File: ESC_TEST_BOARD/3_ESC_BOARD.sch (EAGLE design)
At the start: 63 parts, among them J3 AVR_SPI_PROG_3X2NS, U2 ATMEGA328P_TQFP

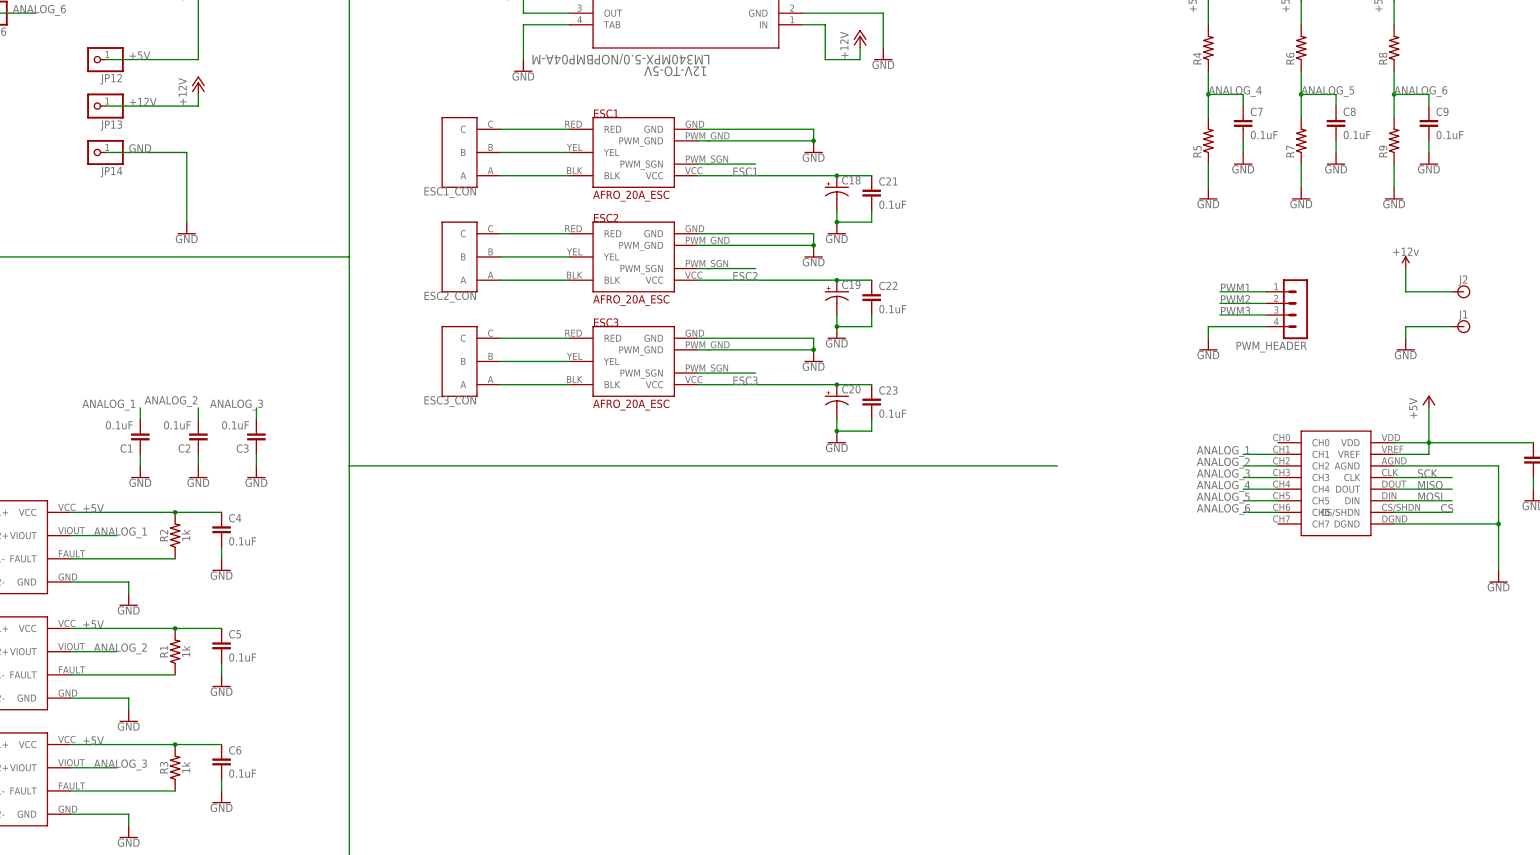
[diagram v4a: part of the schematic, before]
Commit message: Finished routing of Jacobs section
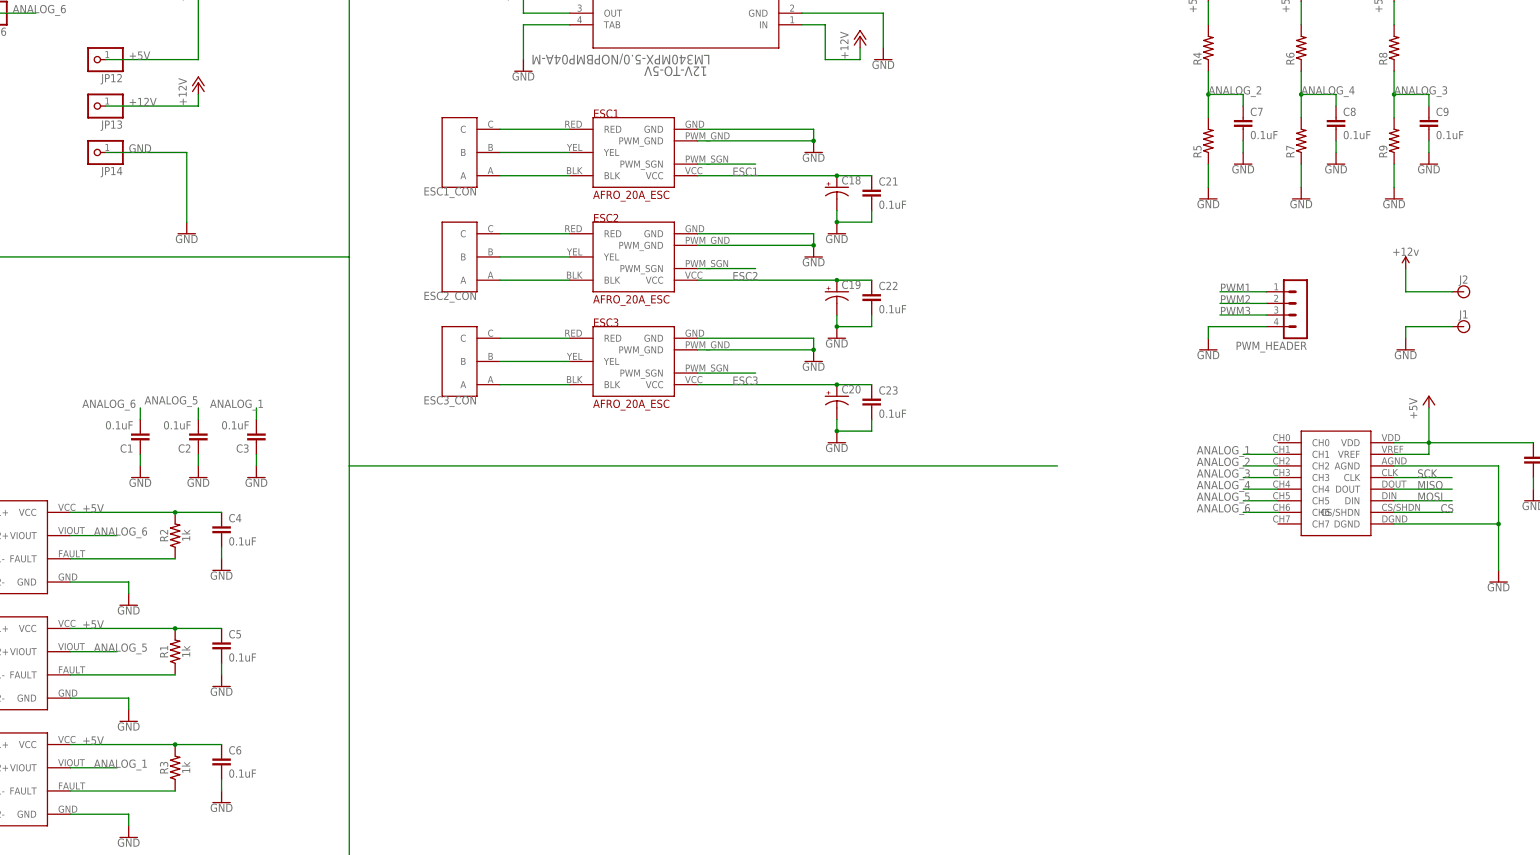
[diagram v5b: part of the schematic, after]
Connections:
- net ANALOG_1: now also C3.2, U$3.VIOUT; no longer C1.2, U$1.VIOUT
- net ANALOG_2: now also C7.1, R4.1, R5.2; no longer C2.2, U$2.VIOUT
- net ANALOG_3: now also C9.1, R8.1, R9.2; no longer C3.2, U$3.VIOUT
- net ANALOG_4: now also C8.1, R6.1, R7.2; no longer C7.1, R4.1, R5.2
- net ANALOG_5: now also C2.2, U$2.VIOUT; no longer C8.1, R6.1, R7.2
- net ANALOG_6: now also C1.2, U$1.VIOUT; no longer C9.1, R8.1, R9.2
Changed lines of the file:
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@@
 <net name="ANALOG_1" class="0">
-<segment>
-<pinref part="U$1" gate="G$1" pin="VIOUT"/>
-<wire x1="60.96" y1="86.36" x2="71.12" y2="86.36" width="0.1524" layer="91"/>
-<label x="66.04" y="86.36" size="1.778" layer="95"/>
-</segment>
 <segment>
 <pinref part="U$4" gate="G$1" pin="CH1"/>
@@
 </segment>
 <segment>
-<pinref part="C1" gate="G$1" pin="2"/>
-<wire x1="76.2" y1="111.76" x2="76.2" y2="114.3" width="0.1524" layer="91"/>
-<label x="63.5" y="114.3" size="1.778" layer="95"/>
+<pinref part="U$3" gate="G$1" pin="VIOUT"/>
+<wire x1="60.96" y1="35.56" x2="71.12" y2="35.56" width="0.1524" layer="91"/>
+<label x="66.04" y="35.56" size="1.778" layer="95"/>
+</segment>
+<segment>
+<pinref part="C3" gate="G$1" pin="2"/>
+<wire x1="101.6" y1="111.76" x2="101.6" y2="114.3" width="0.1524" layer="91"/>
+<label x="91.44" y="114.3" size="1.778" layer="95"/>
 </segment>
 </net>
 <net name="ANALOG_2" class="0">
-<segment>
-<pinref part="U$2" gate="G$1" pin="VIOUT"/>
-<wire x1="60.96" y1="60.96" x2="71.12" y2="60.96" width="0.1524" layer="91"/>
-<label x="66.04" y="60.96" size="1.778" layer="95"/>
-</segment>
-<segment>
-<pinref part="C2" gate="G$1" pin="2"/>
-<wire x1="88.9" y1="111.76" x2="88.9" y2="114.3" width="0.1524" layer="91"/>
-<label x="88.9" y="116.84" size="1.778" layer="95" rot="R180"/>
-</segment>
 <segment>
 <pinref part="U$4" gate="G$1" pin="CH2"/>
@@
 <label x="22.86" y="190.5" size="1.778" layer="95"/>
 </segment>
+<segment>
+<pinref part="R4" gate="G$1" pin="1"/>
+<pinref part="R5" gate="G$1" pin="2"/>
+<wire x1="309.88" y1="187.96" x2="309.88" y2="182.88" width="0.1524" layer="91"/>
+<wire x1="309.88" y1="182.88" x2="309.88" y2="177.8" width="0.1524" layer="91"/>
+<wire x1="309.88" y1="182.88" x2="317.5" y2="182.88" width="0.1524" layer="91"/>
+<junction x="309.88" y="182.88"/>
+<label x="309.88" y="182.88" size="1.778" layer="95"/>
+<pinref part="C7" gate="G$1" pin="1"/>
+<wire x1="317.5" y1="180.34" x2="317.5" y2="182.88" width="0.1524" layer="91"/>
+</segment>
 </net>
 <net name="ANALOG_3" class="0">
-<segment>
-<pinref part="U$3" gate="G$1" pin="VIOUT"/>
-<wire x1="60.96" y1="35.56" x2="71.12" y2="35.56" width="0.1524" layer="91"/>
-<label x="66.04" y="35.56" size="1.778" layer="95"/>
-</segment>
-<segment>
-<pinref part="C3" gate="G$1" pin="2"/>
-<wire x1="101.6" y1="111.76" x2="101.6" y2="114.3" width="0.1524" layer="91"/>
-<label x="91.44" y="114.3" size="1.778" layer="95"/>
-</segment>
 <segment>
 <pinref part="U$4" gate="G$1" pin="CH3"/>
@@
 <wire x1="17.78" y1="180.34" x2="27.94" y2="180.34" width="0.1524" layer="91"/>
 <label x="22.86" y="180.34" size="1.778" layer="95"/>
+</segment>
+<segment>
+<pinref part="R8" gate="G$1" pin="1"/>
+<pinref part="R9" gate="G$1" pin="2"/>
+<wire x1="350.52" y1="187.96" x2="350.52" y2="182.88" width="0.1524" layer="91"/>
+<wire x1="350.52" y1="182.88" x2="350.52" y2="177.8" width="0.1524" layer="91"/>
+<wire x1="350.52" y1="182.88" x2="358.14" y2="182.88" width="0.1524" layer="91"/>
+<junction x="350.52" y="182.88"/>
+<label x="350.52" y="182.88" size="1.778" layer="95"/>
+<pinref part="C9" gate="G$1" pin="1"/>
+<wire x1="358.14" y1="180.34" x2="358.14" y2="182.88" width="0.1524" layer="91"/>
 </segment>
 </net>
@@
 <net name="ANALOG_4" class="0">
 <segment>
-<pinref part="R4" gate="G$1" pin="1"/>
-<pinref part="R5" gate="G$1" pin="2"/>
-<wire x1="309.88" y1="187.96" x2="309.88" y2="182.88" width="0.1524" layer="91"/>
-<wire x1="309.88" y1="182.88" x2="309.88" y2="177.8" width="0.1524" layer="91"/>
-<wire x1="309.88" y1="182.88" x2="317.5" y2="182.88" width="0.1524" layer="91"/>
-<junction x="309.88" y="182.88"/>
-<label x="309.88" y="182.88" size="1.778" layer="95"/>
-<pinref part="C7" gate="G$1" pin="1"/>
-<wire x1="317.5" y1="180.34" x2="317.5" y2="182.88" width="0.1524" layer="91"/>
-</segment>
-<segment>
 <pinref part="U$4" gate="G$1" pin="CH4"/>
 <wire x1="325.12" y1="96.52" x2="317.5" y2="96.52" width="0.1524" layer="91"/>
@@
 <label x="22.86" y="170.18" size="1.778" layer="95"/>
 </segment>
-</net>
-<net name="ANALOG_5" class="0">
 <segment>
 <pinref part="R6" gate="G$1" pin="1"/>
@@
 <wire x1="337.82" y1="180.34" x2="337.82" y2="182.88" width="0.1524" layer="91"/>
 </segment>
+</net>
+<net name="ANALOG_5" class="0">
 <segment>
 <pinref part="U$4" gate="G$1" pin="CH5"/>
@@
 <label x="22.86" y="160.02" size="1.778" layer="95"/>
 </segment>
+<segment>
+<pinref part="C2" gate="G$1" pin="2"/>
+<wire x1="88.9" y1="111.76" x2="88.9" y2="114.3" width="0.1524" layer="91"/>
+<label x="88.9" y="116.84" size="1.778" layer="95" rot="R180"/>
+</segment>
+<segment>
+<pinref part="U$2" gate="G$1" pin="VIOUT"/>
+<wire x1="60.96" y1="60.96" x2="71.12" y2="60.96" width="0.1524" layer="91"/>
+<label x="66.04" y="60.96" size="1.778" layer="95"/>
+</segment>
 </net>
 <net name="ANALOG_6" class="0">
-<segment>
-<pinref part="R8" gate="G$1" pin="1"/>
-<pinref part="R9" gate="G$1" pin="2"/>
-<wire x1="350.52" y1="187.96" x2="350.52" y2="182.88" width="0.1524" layer="91"/>
-<wire x1="350.52" y1="182.88" x2="350.52" y2="177.8" width="0.1524" layer="91"/>
-<wire x1="350.52" y1="182.88" x2="358.14" y2="182.88" width="0.1524" layer="91"/>
-<junction x="350.52" y="182.88"/>
-<label x="350.52" y="182.88" size="1.778" layer="95"/>
-<pinref part="C9" gate="G$1" pin="1"/>
-<wire x1="358.14" y1="180.34" x2="358.14" y2="182.88" width="0.1524" layer="91"/>
-</segment>
 <segment>
 <pinref part="U$4" gate="G$1" pin="CH6"/>
@@
 <label x="48.26" y="200.66" size="1.778" layer="95"/>
 </segment>
-</net>
+<segment>
+<pinref part="C1" gate="G$1" pin="2"/>
+<wire x1="76.2" y1="111.76" x2="76.2" y2="114.3" width="0.1524" layer="91"/>
+<label x="63.5" y="114.3" size="1.778" layer="95"/>
+</segment>
+<segment>
+<pinref part="U$1" gate="G$1" pin="VIOUT"/>
+<wire x1="60.96" y1="86.36" x2="71.12" y2="86.36" width="0.1524" layer="91"/>
+<label x="66.04" y="86.36" size="1.778" layer="95"/>
+</segment>
+</net>

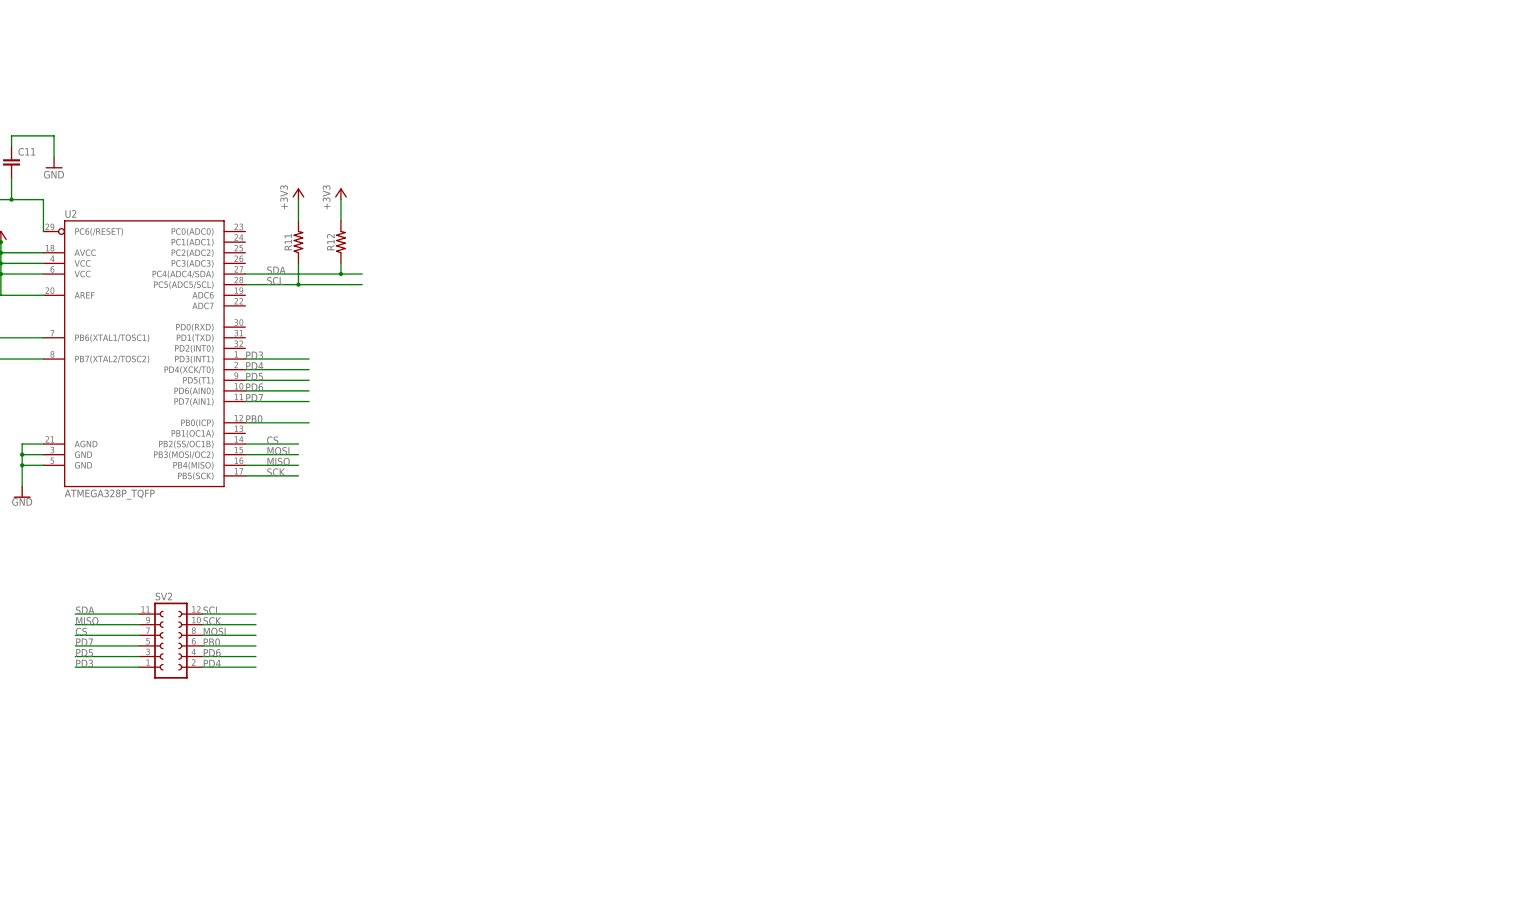
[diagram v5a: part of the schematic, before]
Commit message: Finished adding the raspberry pi portion of the circuit board.
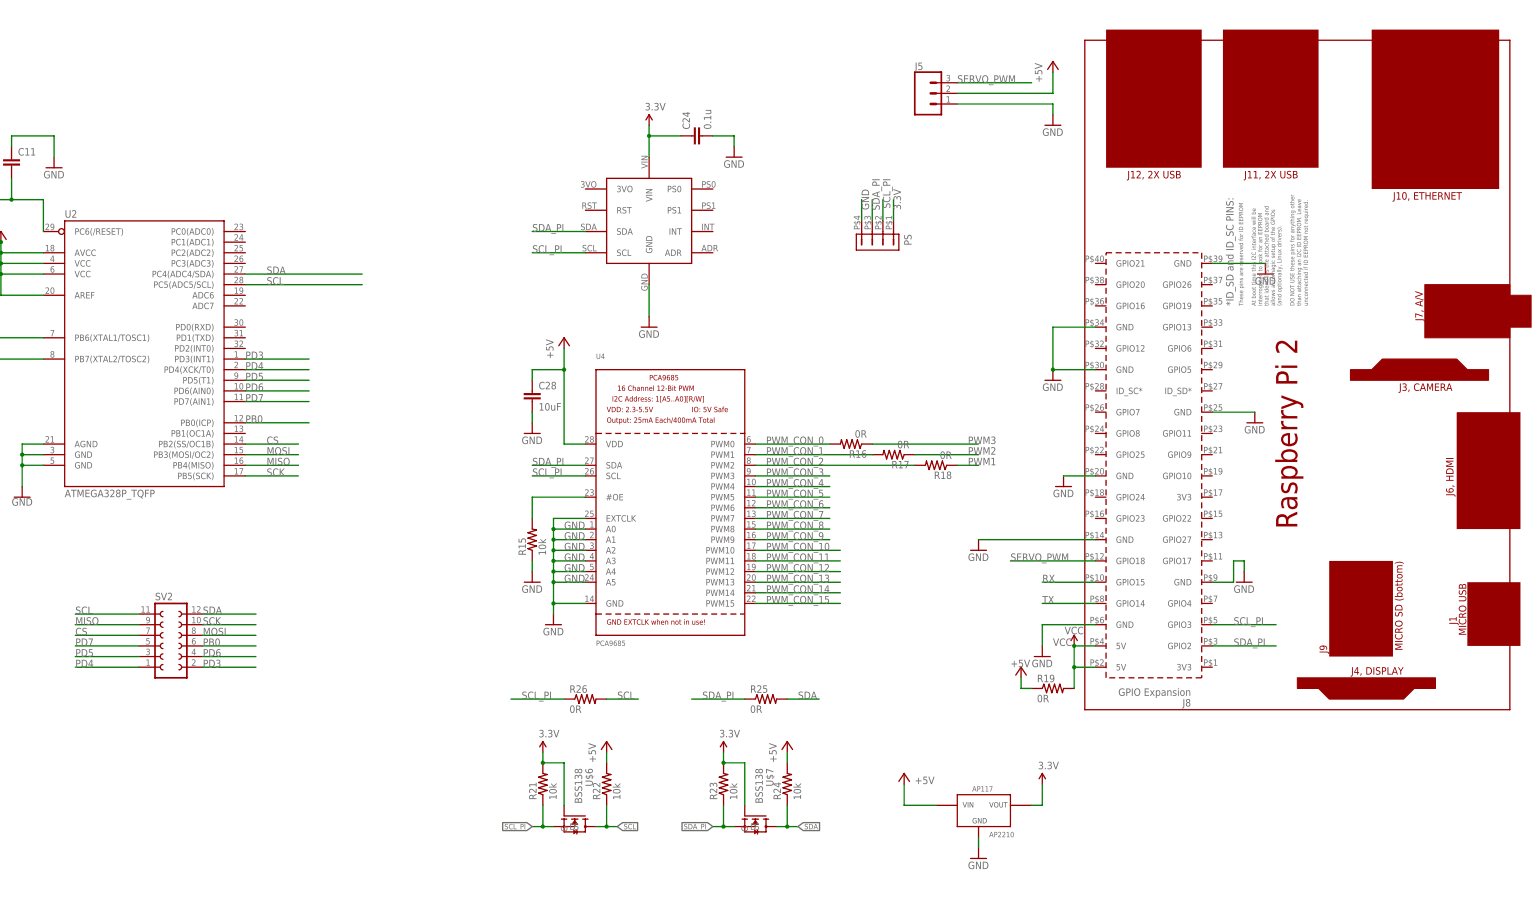
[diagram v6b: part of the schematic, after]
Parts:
- removed R11, R12: (no value), SparkFun-Resistors:RESISTOR0603
- added C24: 0.1u, SparkFun-Passives:CAP0603-CAP
- added C28: 10uF, SparkFun-Capacitors:0.1UF-25V(+80/-20%)(0603)
- added J5: (no value), SparkFun-Connectors:CONN_03
- added PCB1: RPI2, MicrocontrollerComponents:RPI2
- added PS: DF13-4P-1.25DSA, con-hirose-df13:DF13-4P-1.25DSA
- added R15: 10k, SparkFun-Resistors:470OHM1/10W1%(0603)
- added R16, R17, R18: 0R, SparkFun-Resistors:470OHM1/10W1%(0603)
- added R19, R25, R26: 0R, SparkFun-Passives:RESISTOR0603-RES
- added R21, R22, R23, R24: 10k, rcl:R-US_R0603
- added U$5: BNO055_9DOF_BREAKOUT, Other:BNO055_9DOF_BREAKOUT
- added U$6, U$7: BSS138, BSS138:BSS138
- added U$8: AP2210, PowerComponents:AP2210
- added U4: PCA9685, microbuilder:PCA9685
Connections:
- removed net +3V3: R11.2, R12.2
- new net 3.3V: C24.1, PS.1, R21.2, R23.2, U$5.VIN, U$6.G, U$7.G, U$8.VOUT
- new net N$35: R15.2, U4.#OE
- new net PWM_CON_0: R16.2, U4.PWM0
- new net PWM_CON_1: R17.2, U4.PWM1
- new net PWM_CON_10: U4.PWM10
- new net PWM_CON_11: U4.PWM11
- new net PWM_CON_12: U4.PWM12
- new net PWM_CON_13: U4.PWM13
- new net PWM_CON_14: U4.PWM14
- new net PWM_CON_15: U4.PWM15
- new net PWM_CON_2: R18.2, U4.PWM2
- new net PWM_CON_3: U4.PWM3
- new net PWM_CON_4: U4.PWM4
- new net PWM_CON_5: U4.PWM5
- new net PWM_CON_6: U4.PWM6
- new net PWM_CON_7: U4.PWM7
- new net PWM_CON_8: U4.PWM8
- new net PWM_CON_9: U4.PWM9
- new net RX: PCB1.GPIO15
- new net SCL_PI: PCB1.GPIO3, PS.2, R21.1, R26.1, U$5.SCL, U$6.S, U4.SCL
- new net SDA_PI: PCB1.GPIO2, PS.3, R23.1, R25.1, U$5.SDA, U$7.S, U4.SDA
- new net SERVO_PWM: J5.3, PCB1.GPIO18
- new net TX: PCB1.GPIO14
- new net VCC: PCB1.5V@2, PCB1.5V@4, R19.2
- net +5V: now also C28.1, J5.2, R19.1, R22.2, R24.2, U$8.VIN, U4.VDD
- net GND: now also C24.2, C28.2, J5.1, PCB1.GND@14, PCB1.GND@20, PCB1.GND@25, PCB1.GND@30, PCB1.GND@34, PCB1.GND@39, PCB1.GND@6, PCB1.GND@9, PS.4, R15.1, U$5.GND, U$8.GND, U4.A0, U4.A1, U4.A2, U4.A3, U4.A4, U4.A5, U4.EXTCLK, U4.GND
- net PD3: now also SV2.2; no longer SV2.1
- net PD4: now also SV2.1; no longer SV2.2
- net PWM1: now also R18.1
- net PWM2: now also R17.1
- net PWM3: now also R16.1
- net SCL: now also R22.1, R26.2, SV2.11, U$6.D; no longer R11.1, SV2.12
- net SDA: now also R24.1, R25.2, SV2.12, U$7.D; no longer R12.1, SV2.11

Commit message: Addressing comments made by Kyle and Carolyn
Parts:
- added C25, C26, C27, C29: 0.1uF, SparkFun-Capacitors:0.1UF-0603-25V-(+80/-20%)
- added C30: 10uF, SparkFun-Capacitors:0.1UF-0603-25V-(+80/-20%)
- added C31, C32, C33: (no value), rcl:C-EUC0603
- added JP10, JP11, JP15, JP16, JP17, JP18, JP19, JP20, JP21, JP22, JP7, JP8, JP9: (no value), pinhead:PINHD-1X1
- added LED1, LED2, LED3: WS2812B5050, microbuilder:WS2812B5050
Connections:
- new net OUT1: LED1.DO, LED2.DI
- new net OUT2: LED2.DO, LED3.DI
- new net OUT3: LED3.DO
- net +12V: now also C29.2, C30.2
- net +5V: now also C25.1, C27.2, C31.1, C32.1, C33.1, LED1.VDD, LED2.VDD, LED3.VDD
- net 3.3V: now also C26.1
- net GND: now also C25.2, C26.2, C27.1, C29.1, C30.1, C31.2, C32.2, C33.2, LED1.GND, LED2.GND, LED3.GND
- net PD3: now also LED1.DI
- net PWM_CON_10: now also JP20.1
- net PWM_CON_11: now also JP21.1
- net PWM_CON_12: now also JP22.1
- net PWM_CON_13: now also JP9.1
- net PWM_CON_14: now also JP8.1
- net PWM_CON_15: now also JP7.1
- net PWM_CON_3: now also JP10.1
- net PWM_CON_4: now also JP11.1
- net PWM_CON_5: now also JP15.1
- net PWM_CON_6: now also JP16.1
- net PWM_CON_7: now also JP17.1
- net PWM_CON_8: now also JP18.1
- net PWM_CON_9: now also JP19.1
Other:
- note added: "Blue Robotics pressure sensor connector"
- note added: "IMU header pin connector"
- note added: "NEO pixels"
- note added: "PWM, +5V, and GND for servo input"
- note added: "Resistor to connect raspberry pi +5V to main systems +5V. Only bridge this if the +12V to +5V linear regulator is desoldered"
- note added: "Resistor used to bridge both sides if it is found that a logic level converter is not needed"
- note added: "Sparkfun logic level conveter"
- moved on the sheet: C24, C28, R15, R16, R17, R18, R21, R22, R23, R24, R25, R26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
